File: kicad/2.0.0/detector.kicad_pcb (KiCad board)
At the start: 2 copper layers, 65 parts, among them U1 LM317, U2 LM337, U3 REF5010ID, U4 OPA2197xD, U5 OPA2197xD

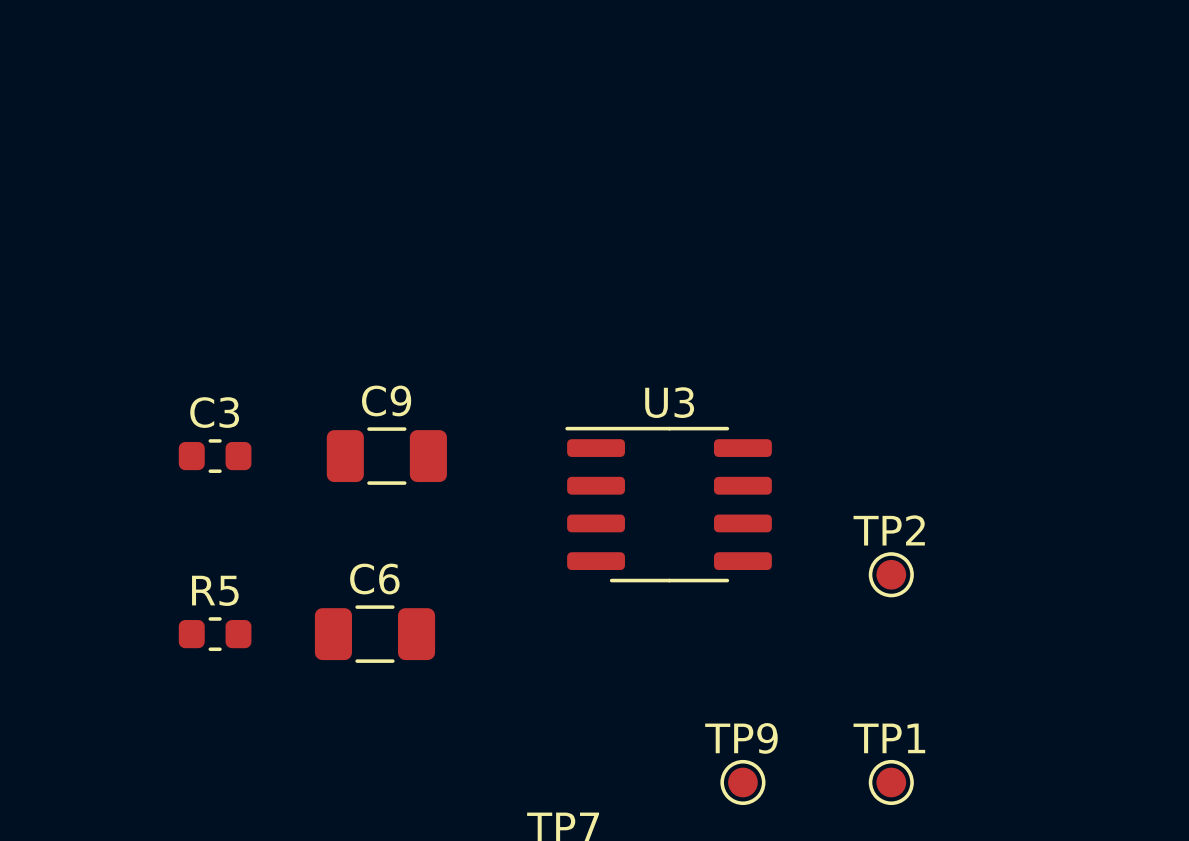
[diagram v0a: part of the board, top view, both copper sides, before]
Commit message: routed REF5010 tracks for 2.0.0 detector board
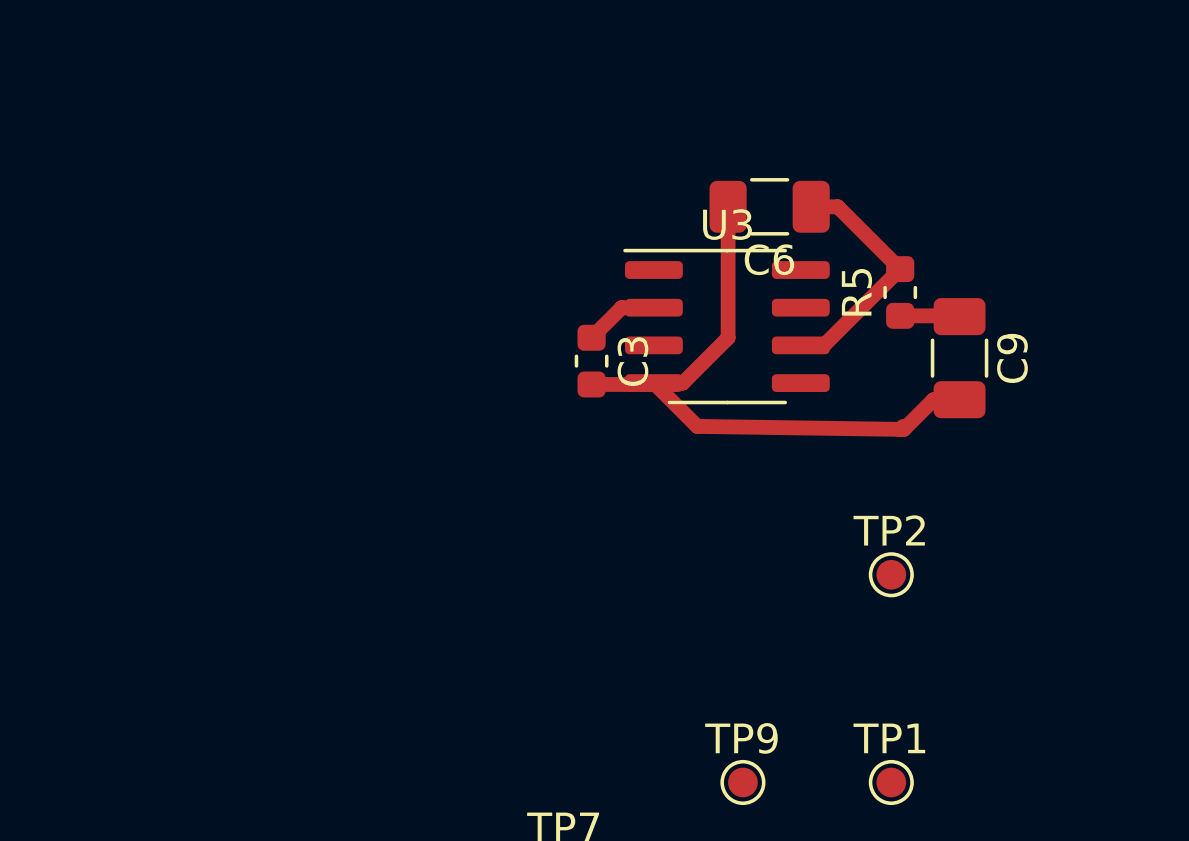
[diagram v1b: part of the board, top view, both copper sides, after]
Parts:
- moved R5 25.8 mm to (178.3, 32.5), turned to 90 degrees
- moved C6 19.6 mm to (173.9, 29.6), turned to 180 degrees
- moved C9 19.6 mm to (180.3, 34.7), turned to 270 degrees
- moved C3 13.1 mm to (167.9, 34.8), turned to 270 degrees
- moved U3 6.31 mm to (172.5, 33.6)
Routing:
- net GND: track 0.00 -> 21.1 mm
- net Net-(C6-Pad1): track 0.00 -> 8.28 mm
- net +12V: track 0.00 -> 2.52 mm
- net Net-(C9-Pad1): track 0.00 -> 2.01 mm

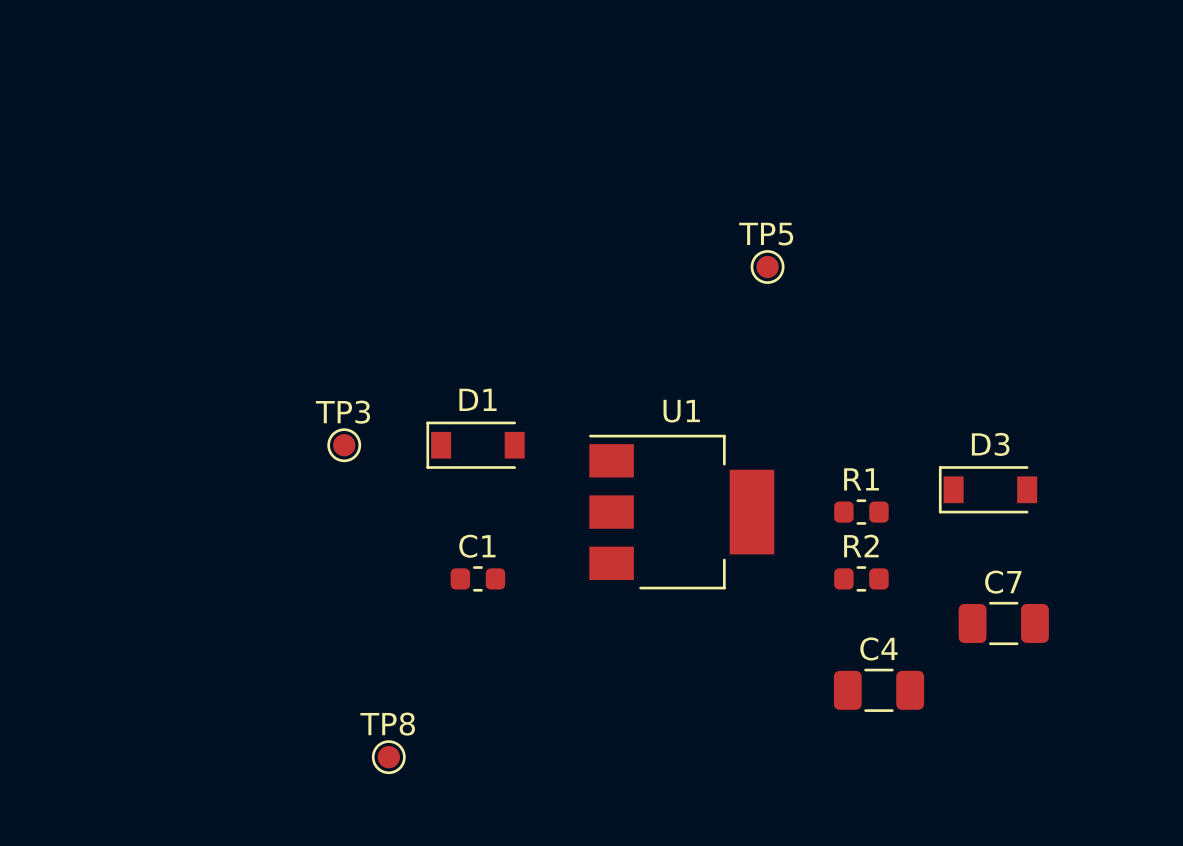
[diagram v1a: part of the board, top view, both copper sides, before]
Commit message: routed tracks for LM317 on 2.0.0 detector
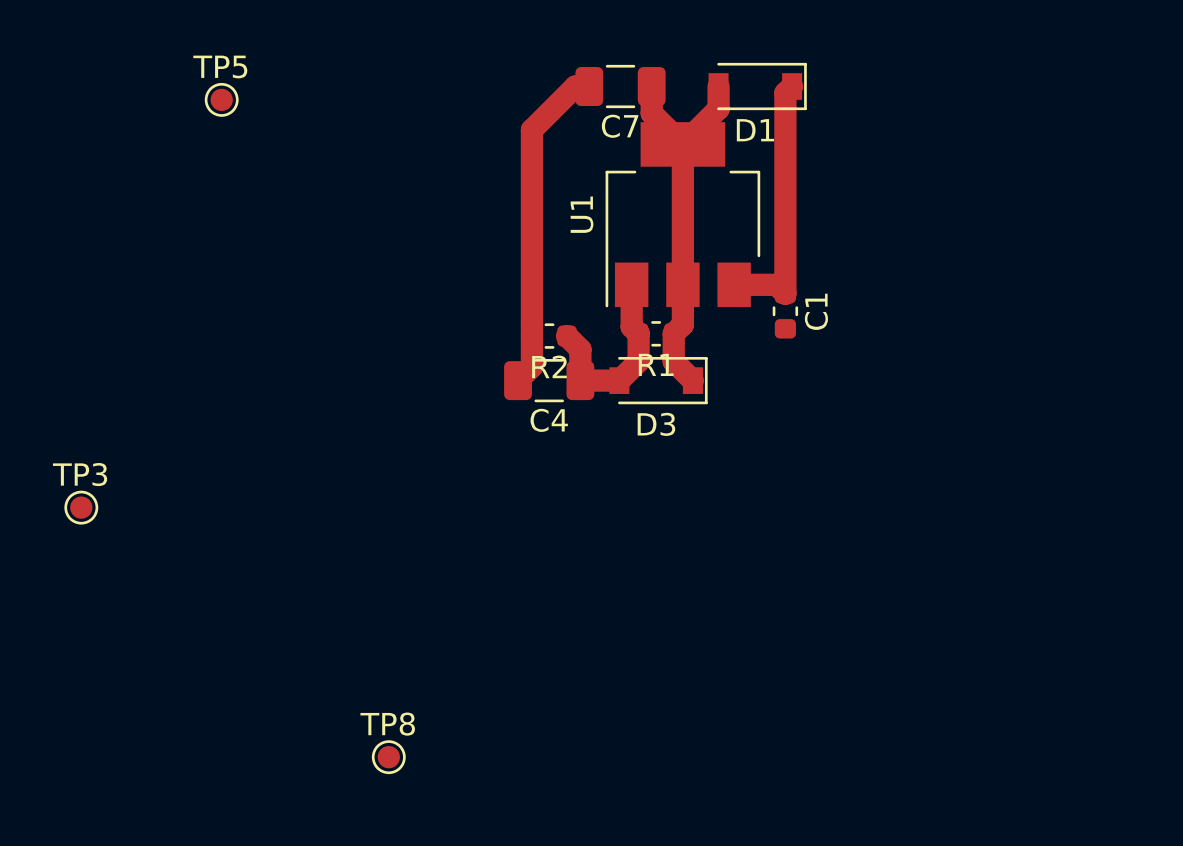
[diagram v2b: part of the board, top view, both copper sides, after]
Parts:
- moved C7 29.6 mm to (116.4, 15.9), turned to 180 degrees
- moved TP5 25.6 mm to (98.5, 16.5)
- moved D1 20.4 mm to (122.5, 15.9), turned to 180 degrees
- moved C4 20.3 mm to (113.2, 29.1), turned to 180 degrees
- moved C1 18.3 mm to (123.8, 26.0), turned to 270 degrees
- moved R2 17.7 mm to (113.2, 27.1), turned to 180 degrees
- moved D3 15.8 mm to (118.0, 29.1), turned to 180 degrees
- moved U1 13.4 mm to (119.2, 21.6), turned to 90 degrees
- moved R1 12.2 mm to (118.0, 27.0), turned to 180 degrees
- moved TP3 12.1 mm to (92.2, 34.8)
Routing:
- net +12V: track 2.52 -> 20.1 mm
- net GND: track 21.1 -> 36.0 mm
- net +15V: track 0.00 -> 11.9 mm
- net Net-(C4-Pad1): track 0.00 -> 8.79 mm

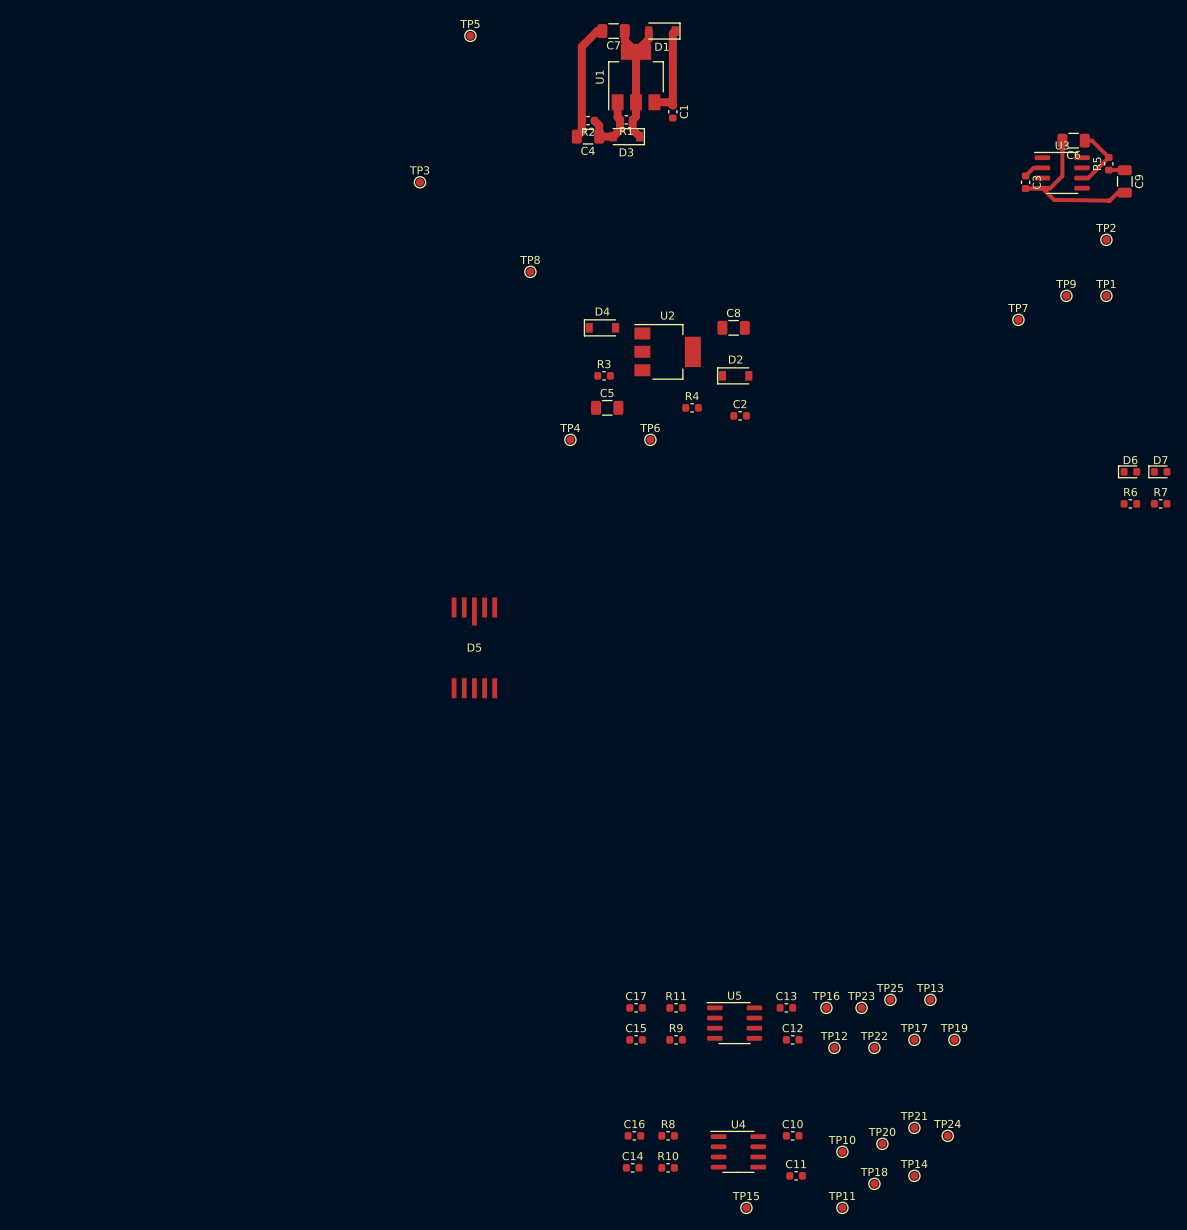
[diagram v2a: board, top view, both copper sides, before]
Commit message: completed tracks of voltage references and regulators of 2.0.0 detector
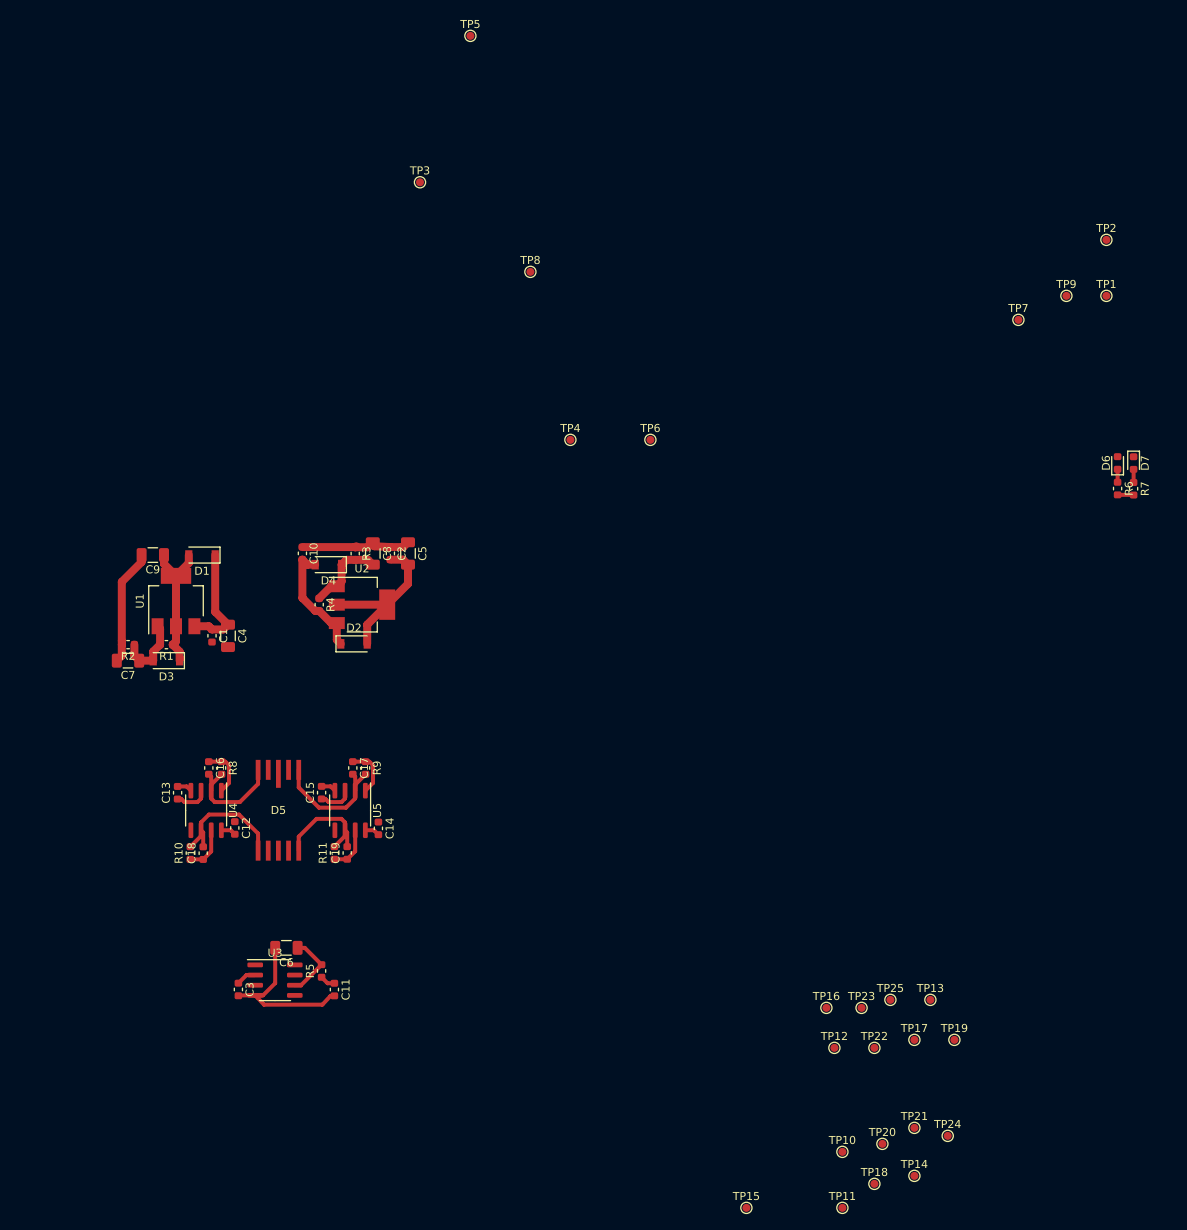
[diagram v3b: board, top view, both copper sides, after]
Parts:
- added C18: 18p, Capacitor_SMD:C_0603_1608Metric, F.Cu at (65.1, 118.7)
- added C19: 18p, Capacitor_SMD:C_0603_1608Metric, F.Cu at (83.1, 118.6)
- C1, C2: value 100n -> 10u
- C10, C11: value 100n -> 22u
- C14, C15: value 18p -> 100n
- C4, C5: value 10u -> 100n
- C7, C8: value 22u -> 10u
- D1, D2: value D_Small -> SOT-123
- TP5: value +12V -> +10V
- TP6: value -12V -> +12V
- TP7: value +10V -> -12V
- moved C3 140.9 mm to (69.5, 135.7)
- moved C6 140.9 mm to (75.5, 130.5)
- moved R5 140.9 mm to (79.9, 133.4)
- moved U3 140.9 mm to (74.1, 134.5)
- moved C9 130.2 mm to (58.8, 81.4), turned to 180 degrees
- moved C7 99.4 mm to (55.7, 94.6)
- moved C10 95.2 mm to (77.5, 81.2), turned to 270 degrees
- moved R1 87.2 mm to (60.5, 92.6)
- moved C1 87.2 mm to (66.2, 91.5)
- moved D1 87.2 mm to (65.0, 81.4)
- moved D3 87.2 mm to (60.5, 94.6)
- moved R2 87.2 mm to (55.7, 92.6)
- moved U1 87.2 mm to (61.7, 87.2)
- moved C13 80.7 mm to (61.9, 111.1), turned to 90 degrees
- moved U4 79.0 mm to (65.5, 113.3), turned to 270 degrees
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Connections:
- C10 pad 2: +12V -> -12V
- C11 pad 1: GND -> Net-(C11-Pad1)
- C11 pad 2: -12V -> GND
- C14 pad 1: /-X1 -> GND
- C14 pad 2: Net-(C14-Pad2) -> +12V
- C15 pad 1: /-Y1 -> GND
- C15 pad 2: Net-(C15-Pad2) -> -12V
- C16 pad 1: /-Y2 -> /-X1
- C17 pad 1: /-X2 -> /-Y1
- C4 pad 1: Net-(C4-Pad1) -> +15V
- C5 pad 2: Net-(C5-Pad2) -> -15V
- C7 pad 1: +12V -> Net-(C7-Pad1)
- C8 pad 2: -12V -> Net-(C8-Pad2)
- C9 pad 1: Net-(C9-Pad1) -> +12V
- D3 pad 2: Net-(C4-Pad1) -> Net-(C7-Pad1)
- D4 pad 1: Net-(C5-Pad2) -> Net-(C8-Pad2)
- D5 pad 1: Net-(C14-Pad2) -> Net-(C16-Pad2)
- D5 pad 10: Net-(C16-Pad2) -> Net-(C18-Pad2)
- D5 pad 5: Net-(C15-Pad2) -> Net-(C17-Pad2)
- D5 pad 6: Net-(C17-Pad2) -> Net-(C19-Pad2)
- D5 pad 8: Net-(C9-Pad1) -> Net-(C11-Pad1)
- R1 pad 2: Net-(C4-Pad1) -> Net-(C7-Pad1)
- R10 pad 2: Net-(C16-Pad2) -> Net-(C18-Pad2)
- R11 pad 2: Net-(C17-Pad2) -> Net-(C19-Pad2)
- R2 pad 1: Net-(C4-Pad1) -> Net-(C7-Pad1)
- R3 pad 2: Net-(C5-Pad2) -> Net-(C8-Pad2)
- R4 pad 1: Net-(C5-Pad2) -> Net-(C8-Pad2)
- R5 pad 1: Net-(C9-Pad1) -> Net-(C11-Pad1)
- R8 pad 2: Net-(C14-Pad2) -> Net-(C16-Pad2)
- R9 pad 2: Net-(C15-Pad2) -> Net-(C17-Pad2)
- TP14 pad 1: Net-(C14-Pad2) -> Net-(C16-Pad2)
- TP16 pad 1: Net-(C15-Pad2) -> Net-(C17-Pad2)
- TP20 pad 1: Net-(C16-Pad2) -> Net-(C18-Pad2)
- TP22 pad 1: Net-(C17-Pad2) -> Net-(C19-Pad2)
- TP5 pad 1: +12V -> Net-(C6-Pad1)
- TP6 pad 1: -12V -> +12V
- TP7 pad 1: Net-(C6-Pad1) -> -12V
- TP9 pad 1: Net-(C9-Pad1) -> Net-(C11-Pad1)
- U1 pad 1: Net-(C4-Pad1) -> Net-(C7-Pad1)
- U2 pad 1: Net-(C5-Pad2) -> Net-(C8-Pad2)
- U4 pad 2: Net-(C14-Pad2) -> Net-(C16-Pad2)
- U4 pad 6: Net-(C16-Pad2) -> Net-(C18-Pad2)
- U5 pad 2: Net-(C15-Pad2) -> Net-(C17-Pad2)
- U5 pad 6: Net-(C17-Pad2) -> Net-(C19-Pad2)
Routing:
- net GND: track 36.0 -> 59.8 mm
- net -15V: track 0.00 -> 20.8 mm
- net -12V: track 0.00 -> 18.8 mm
- net Net-(C17-Pad2): track 0.00 -> 16.5 mm
- net Net-(C18-Pad2): track 0.00 -> 16.4 mm
- net Net-(C16-Pad2): track 0.00 -> 14.5 mm
- net Net-(C19-Pad2): track 0.00 -> 14.4 mm
- net Net-(C8-Pad2): track 0.00 -> 10.2 mm
- net Net-(C4-Pad1): track 8.79 -> 0.00 mm
- net Net-(C7-Pad1): track 0.00 -> 8.79 mm
- net /-Y1: track 0.00 -> 6.28 mm
- net /-X1: track 0.00 -> 6.28 mm
- net /-Y2: track 0.00 -> 5.68 mm
- net /-X2: track 0.00 -> 5.64 mm
- net +12V: track 20.1 -> 23.9 mm
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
